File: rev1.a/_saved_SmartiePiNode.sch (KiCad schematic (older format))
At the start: 48 parts, among them CN1 USBMICROb, CN2 ST-LINK, CN3 SX1238_TRX_HEADER, SW1 SW_PUSH, U1 ISL91127IR, U2 STM32L052_LQFP48, X1 8MHz(16pF), X2 ABS25-32.768KHZ-6-T

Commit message: started footprint generation
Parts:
- C1, C10, C11, C12, C13, C14, C15, C16, C17, C18, C19, C2, C3, C4, C5, C6, C7, C8, C9: footprint (none) -> Capacitors_SMD:C_0603
- CN2: footprint (none) -> Pin_Headers:Pin_Header_Straight_1x05
- CN3: footprint (none) -> Pin_Headers:Pin_Header_Straight_2x10
- R1, R10, R11, R12, R13, R14, R2, R3, R4, R5, R6, R7, R8, R9: footprint (none) -> Resistors_SMD:R_0603
- SD1: footprint MF_Connectors_MF-MICROSD -> (none)
- U2: footprint (none) -> Housings_QFP:LQFP-48_7x7mm_Pitch0.5mm

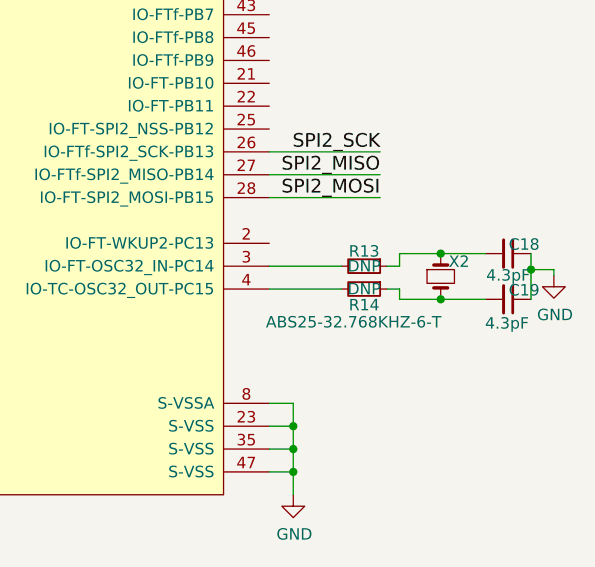
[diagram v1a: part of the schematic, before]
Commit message: intersil isl91127ir footprint and 3d model
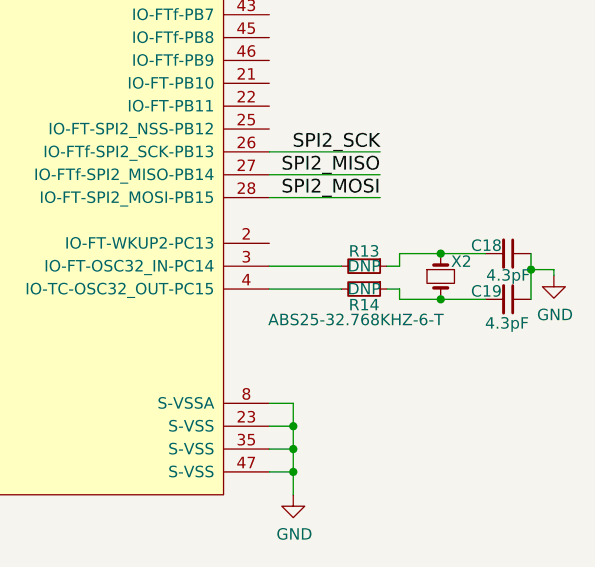
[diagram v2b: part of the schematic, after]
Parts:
- removed X2: ABS25-32.768KHZ-6-T, symbol Crystal_Small
- added X2: ABS25-32.768KHZ-6-T, abracon-abs07:abracon-abs07, symbol abracon-abs25
- BT1: footprint (none) -> mpd-bh123a:mpd-BH123A
- CN1: footprint (none) -> amphenol-microusb-10118194:amphenol-microusb-10118194
- D1, D2: footprint (none) -> Diodes_SMD:SOD-123
- F1: footprint (none) -> belfuse-c2q:belfuse-c2q
- L1: footprint (none) -> murata-1277AS-H-1R0M:murata-1277AS-H-1R0M
- L2: footprint (none) -> bourns-MH1608-601Y:MH1608-601Y
- SD1: footprint (none) -> amphenol-microsd-114-00841-68:amphenol-microsd-1140084168
- SW1: footprint (none) -> te-1825966-1:SWITCH_1825966_1
- U1: footprint (none) -> intersil-isl91127ir:intersil-isl91127ir
- U2: footprint Housings_QFP:LQFP-48_7x7mm_Pitch0.5mm -> st-stm32l052-lqfp48:STM32L052C8T6
- X1: footprint (none) -> abracon-abm10:abracon-abm10
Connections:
- net at C19.2, R14.1: now also X2.1
- net at C18.2, R13.1: now also X2.2
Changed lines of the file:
@@
 LIBS:sw-push
 LIBS:micro-sd-card
+LIBS:crystal_small
 LIBS:SmartiePiNode-cache
 EELAYER 26 0
@@
 F 0 "U1" H 3065 5695 60  0000 C CNN
 F 1 "ISL91127IR" H 3520 7105 60  0000 C CNN
-F 2 "" H 3520 6400 60  0001 C CNN
+F 2 "intersil-isl91127ir:intersil-isl91127ir" H 3520 6400 60  0001 C CNN
 F 3 "" H 3520 6400 60  0001 C CNN
 	1    3520 6400
@@
 F 0 "L1" V 3565 5480 50  0000 C CNN
 F 1 "1uH" V 3460 5485 50  0000 C CNN
-F 2 "" H 3500 5480 50  0001 C CNN
+F 2 "murata-1277AS-H-1R0M:murata-1277AS-H-1R0M" H 3500 5480 50  0001 C CNN
 F 3 "" H 3500 5480 50  0001 C CNN
 	1    3500 5480
@@
 F 0 "U2" H 7620 -460 60  0000 C CNN
 F 1 "STM32L052_LQFP48" H 8615 2530 60  0000 C CNN
-F 2 "Housings_QFP:LQFP-48_7x7mm_Pitch0.5mm" H 7875 1690 60  0001 C CNN
+F 2 "st-stm32l052-lqfp48:STM32L052C8T6" H 7875 1690 60  0001 C CNN
 F 3 "" H 7875 1690 60  0001 C CNN
 	1    7875 1690
@@
 F 0 "CN1" H 1230 4760 60  0000 R CNN
 F 1 "USBMICROb" H 1435 4160 60  0000 R CNN
-F 2 "" H 1165 4460 60  0001 C CNN
+F 2 "amphenol-microusb-10118194:amphenol-microusb-10118194" H 1165 4460 60  0001 C CNN
 F 3 "" H 1165 4460 60  0000 C CNN
 	1    1165 4460
@@
 F 0 "SW1" H 6055 3085 50  0000 C CNN
 F 1 "SW_PUSH" H 6195 2930 50  0000 C CNN
-F 2 "" H 6180 2990 60  0001 C CNN
+F 2 "te-1825966-1:SWITCH_1825966_1" H 6180 2990 60  0001 C CNN
 F 3 "" H 6180 2990 60  0000 C CNN
 	1    6180 2990
@@
 F 0 "X1" V 6745 2780 50  0000 L CNN
 F 1 "8MHz(16pF)" V 6960 2595 50  0000 L CNN
-F 2 "" H 6815 2740 50  0001 C CNN
+F 2 "abracon-abm10:abracon-abm10" H 6815 2740 50  0001 C CNN
 F 3 "" H 6815 2740 50  0001 C CNN
 	1    6815 2740
@@
 Wire Wire Line
 	10140 2790 9825 2790
-$Comp
-L Crystal_Small X2
-U 1 1 5B098328
-P 10575 2835
-F 0 "X2" V 10510 2870 50  0000 L CNN
-F 1 "ABS25-32.768KHZ-6-T" V 10775 2070 50  0000 L CNN
-F 2 "" H 10575 2835 50  0001 C CNN
-F 3 "" H 10575 2835 50  0001 C CNN
-	1    10575 2835
-	0    1    1    0
-$EndComp
 Wire Wire Line
 	10340 2890 10395 2890
@@
 U 1 1 5B098883
 P 10870 2735
-F 0 "C18" V 10830 2805 50  0000 C CNN
+F 0 "C18" V 10835 2640 50  0000 C CNN
 F 1 "4.3pF" V 10965 2735 50  0000 C CNN
 F 2 "Capacitors_SMD:C_0603" H 10870 2735 50  0001 C CNN
@@
 U 1 1 5B098936
 P 10870 2935
-F 0 "C19" V 10830 3005 50  0000 C CNN
+F 0 "C19" V 10835 2840 50  0000 C CNN
 F 1 "4.3pF" V 10975 2930 50  0000 C CNN
 F 2 "Capacitors_SMD:C_0603" H 10870 2935 50  0001 C CNN
@@
 F 0 "SD1" H 870 -200 45  0000 C CNN
 F 1 "SD_CARD_SLOT_MICRO" H 1125 960 45  0000 C CNN
-F 2 "" H 845 1065 20  0001 C CNN
+F 2 "amphenol-microsd-114-00841-68:amphenol-microsd-1140084168" H 845 1065 20  0001 C CNN
 F 3 "" H 815 915 60  0000 C CNN
 	1    815  915
@@
 F 0 "BT1" V 1380 3135 50  0000 L CNN
 F 1 "CR123A" V 1650 3070 50  0000 L CNN
-F 2 "" V 1525 3220 50  0001 C CNN
+F 2 "mpd-bh123a:mpd-BH123A" V 1525 3220 50  0001 C CNN
 F 3 "" V 1525 3220 50  0001 C CNN
 	1    1525 3160
@@
 F 0 "D2" H 910 6235 50  0000 C CNN
 F 1 "SCHOTTKY" H 860 6080 50  0000 C CNN
-F 2 "" V 910 6150 50  0001 C CNN
+F 2 "Diodes_SMD:SOD-123" V 910 6150 50  0001 C CNN
 F 3 "" V 910 6150 50  0001 C CNN
 	1    910  6150
@@
 F 0 "D1" H 910 6005 50  0000 C CNN
 F 1 "SCHOTTKY" H 840 5850 50  0000 C CNN
-F 2 "" V 910 5920 50  0001 C CNN
+F 2 "Diodes_SMD:SOD-123" V 910 5920 50  0001 C CNN
 F 3 "" V 910 5920 50  0001 C CNN
 	1    910  5920
@@
 F 0 "L2" V 7775 5330 50  0000 C CNN
 F 1 "ferrite" V 7875 5330 50  0000 C CNN
-F 2 "" H 7825 5330 50  0001 C CNN
+F 2 "bourns-MH1608-601Y:MH1608-601Y" H 7825 5330 50  0001 C CNN
 F 3 "" H 7825 5330 50  0001 C CNN
 	1    7825 5330
@@
 F 0 "F1" H 1380 6095 50  0000 C CNN
 F 1 "500mA" H 1380 6205 50  0000 C CNN
-F 2 "" H 1380 6150 50  0001 C CNN
+F 2 "belfuse-c2q:belfuse-c2q" H 1380 6150 50  0001 C CNN
 F 3 "" H 1380 6150 50  0001 C CNN
 	1    1380 6150
@@
 Text Notes 5500 5950 0    39   ~ 0
 second stage output filter goes here.
+$Comp
+L abracon-abs25 X2
+U 1 1 5B12A6FF
+P 10575 2835
+F 0 "X2" V 10510 2880 50  0000 L CNN
+F 1 "ABS25-32.768KHZ-6-T" V 10765 2080 50  0000 L CNN
+F 2 "abracon-abs07:abracon-abs07" H 10575 2835 50  0001 C CNN
+F 3 "" H 10575 2835 50  0001 C CNN
+	1    10575 2835
+	0    1    1    0
+$EndComp
 $EndSCHEMATC

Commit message: d1 and d2 schotky diode footprint and 3d models
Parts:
- C1: footprint Capacitors_SMD:C_0603 -> Capacitors_SMD:C_0805
- D1, D2: footprint Diodes_SMD:SOD-123 -> onsemi-NRVB120VLSFT1G:onsemi-NRVB120VLSFT1G
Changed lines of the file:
@@
 F 0 "C1" H 1790 6370 50  0000 L CNN
 F 1 "DNP" H 1790 6240 50  0000 L CNN
-F 2 "Capacitors_SMD:C_0603" H 1785 6305 50  0001 C CNN
+F 2 "Capacitors_SMD:C_0805" H 1785 6305 50  0001 C CNN
 F 3 "" H 1785 6305 50  0001 C CNN
 	1    1785 6305
@@
 F 0 "D2" H 910 6235 50  0000 C CNN
 F 1 "SCHOTTKY" H 860 6080 50  0000 C CNN
-F 2 "Diodes_SMD:SOD-123" V 910 6150 50  0001 C CNN
+F 2 "onsemi-NRVB120VLSFT1G:onsemi-NRVB120VLSFT1G" V 910 6150 50  0001 C CNN
 F 3 "" V 910 6150 50  0001 C CNN
 	1    910  6150
@@
 F 0 "D1" H 910 6005 50  0000 C CNN
 F 1 "SCHOTTKY" H 840 5850 50  0000 C CNN
-F 2 "Diodes_SMD:SOD-123" V 910 5920 50  0001 C CNN
+F 2 "onsemi-NRVB120VLSFT1G:onsemi-NRVB120VLSFT1G" V 910 5920 50  0001 C CNN
 F 3 "" V 910 5920 50  0001 C CNN
 	1    910  5920
